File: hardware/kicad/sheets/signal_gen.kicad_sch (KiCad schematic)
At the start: 32 parts, among them U3 SG-8002CA-PH 25MHz, U4 AD9833BRMZ, U5 OPA1656ID, U6 AD633JRZ-R7, U7 MCP4921-E/SN, U8 LM4040DBZ-2.5, U9 OPA188ID

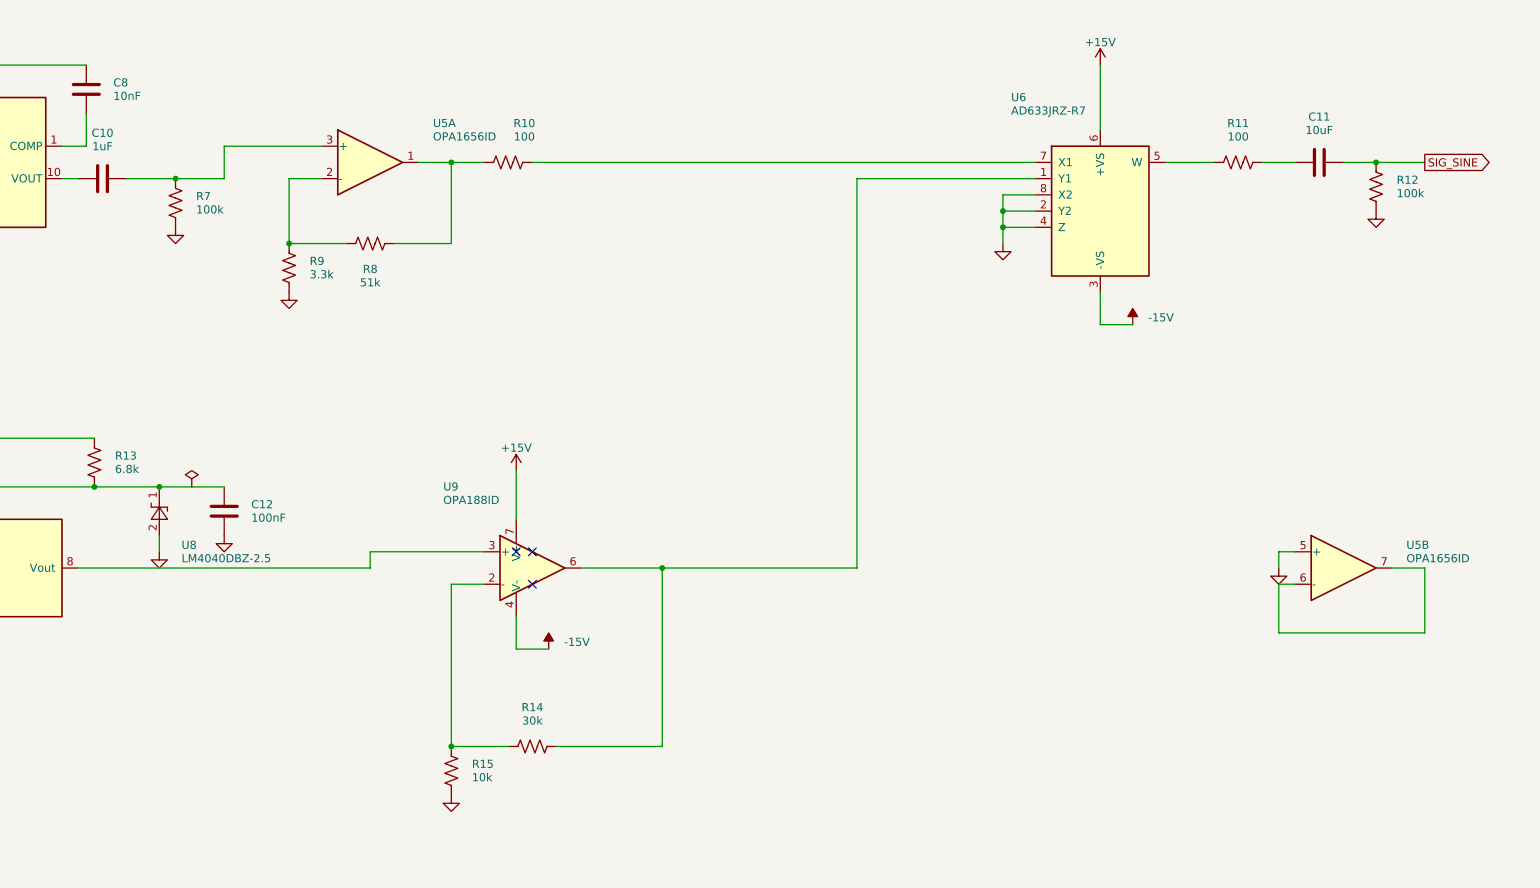
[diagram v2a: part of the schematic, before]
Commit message: KiCad schematic: INA239, ADS1220, SC18IS604 bridge, relay driver, test points
- system_current: INA237 -> INA239 (SPI, CS GPIO3) with the 49.9 ohm / 470 nF
  input filter, power LED and ALERT LED; VBUS shares the filtered IN- node.
- cold_head: ADS122C04 -> ADS1220 (SPI, CS GPIO44).
- i2c_bridge (new): SC18IS604 SPI-to-I2C bridge for the EMC2303, with a
  74LVC1G125 gating its MISO onto the shared bus.
- compressor_relay (new): GPIO16 high-side switch sharing one generator
  function with the amplifier REM switch.
- debug (new): about 40 test points and rail LEDs (the isolated rail LED
  returns to ISO_GND).
- ISO7741 -> ACS37800 SPI lines are straight wires (pins reordered on the
  symbol); USB_VBUS is one wire plus a naming label.
- Custom symbols for INA239, ADS1220, SC18IS604; datasheet rules 117 -> 162;
  GPIO map checks updated. ERC 0.

Co-Authored-By: Claude Sonnet 5.5 <noreply@anthropic.com>
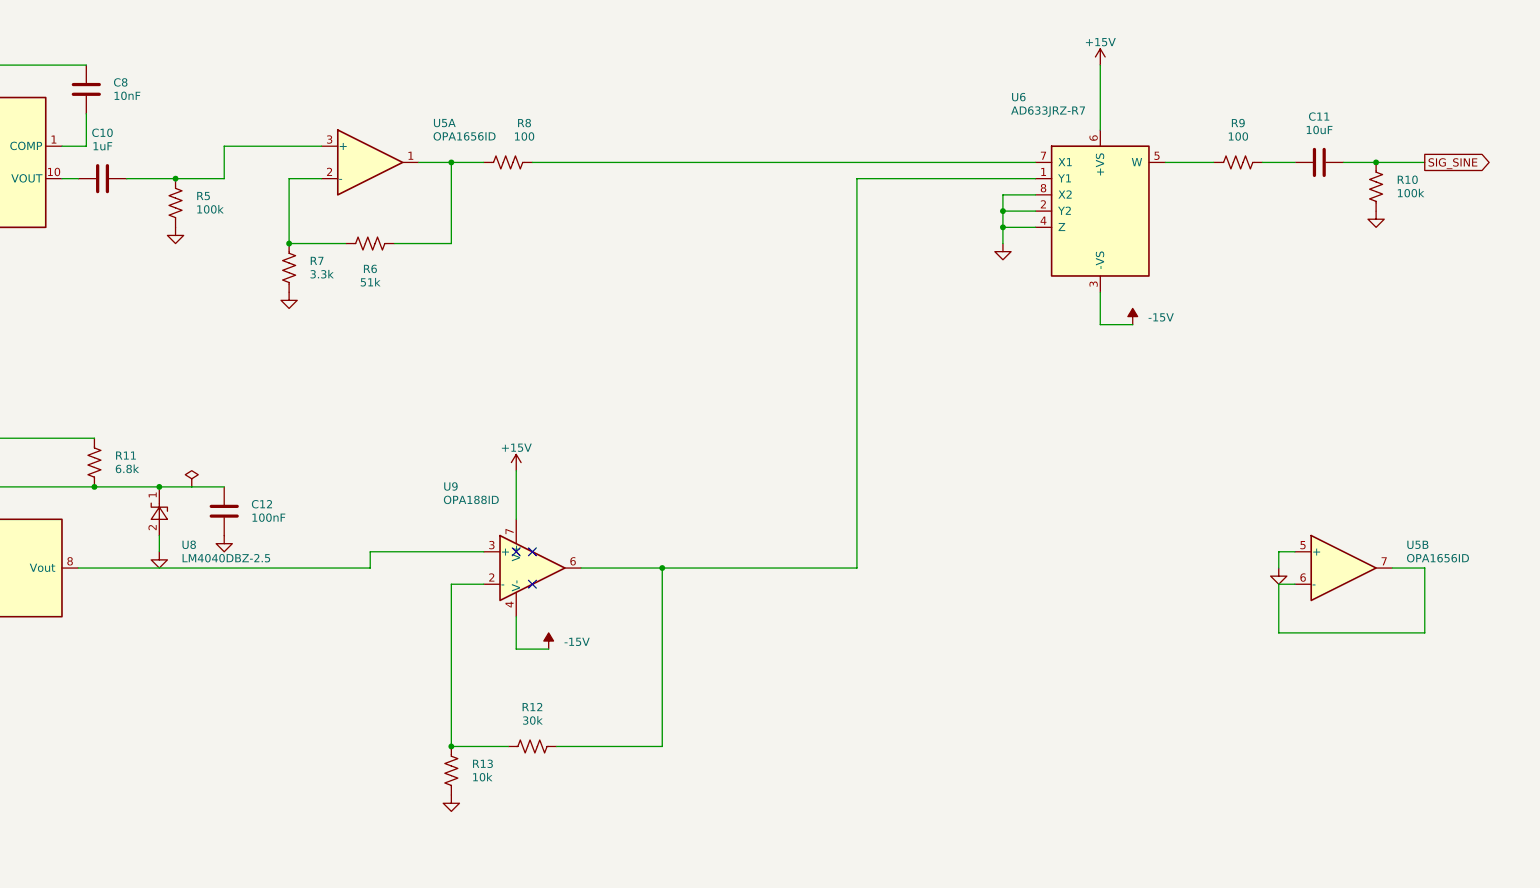
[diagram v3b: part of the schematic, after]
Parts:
- removed C15, C21: 10uF, Capacitor_SMD:C_0805_2012Metric, symbol Device:C
- removed C16, C22: 100nF, Capacitor_SMD:C_0603_1608Metric, symbol Device:C
- removed R14: 30k, Resistor_SMD:R_0603_1608Metric, symbol Device:R_US
- removed R15: 10k, Resistor_SMD:R_0603_1608Metric, symbol Device:R_US
- removed R9: 3.3k, Resistor_SMD:R_0603_1608Metric, symbol Device:R_US
- removed unit 2 of U5
- removed U7: MCP4921-E/SN, Package_SO:SOIC-8_3.9x4.9mm_P1.27mm, symbol cryocooler:MCP4921
- removed U9: OPA188ID, Package_SO:SOIC-8_3.9x4.9mm_P1.27mm, symbol Amplifier_Operational:OPA188xxD
- added C12, C13, C14, C19, C20: 100nF, Capacitor_SMD:C_0603_1608Metric, symbol Device:C
- added C8: 10nF, Capacitor_SMD:C_0603_1608Metric, symbol Device:C
- added R12: 30k, Resistor_SMD:R_0603_1608Metric, symbol Device:R_US
- added U4: AD9833BRMZ, Package_SO:MSOP-10_3x3mm_P0.5mm, symbol Interface:AD9833xRM
- added unit 1 of U5
- added U6: AD633JRZ-R7, Package_SO:SOIC-8_3.9x4.9mm_P1.27mm, symbol cryocooler:AD633JRZ-R7
- C10: renamed from C8; value 10nF -> 1uF; footprint Capacitor_SMD:C_0603_1608Metric -> Capacitor_SMD:C_0805_2012Metric
- C15: renamed from C13; value 100nF -> 10uF; footprint Capacitor_SMD:C_0603_1608Metric -> Capacitor_SMD:C_0805_2012Metric
- C21: renamed from C19; value 100nF -> 10uF; footprint Capacitor_SMD:C_0603_1608Metric -> Capacitor_SMD:C_0805_2012Metric
- C9: renamed from U4; value AD9833BRMZ -> 100nF; footprint Package_SO:MSOP-10_3x3mm_P0.5mm -> Capacitor_SMD:C_0603_1608Metric; symbol Interface:AD9833xRM -> Device:C
- R10: value 100 -> 100k
- R11: renamed from R12; value 100k -> 6.8k
- R13: value 6.8k -> 10k
- R5: renamed from C9; value 100nF -> 100k; footprint Capacitor_SMD:C_0603_1608Metric -> Resistor_SMD:R_0603_1608Metric; symbol Device:C -> Device:R_US
- R6: renamed from C10; value 1uF -> 51k; footprint Capacitor_SMD:C_0805_2012Metric -> Resistor_SMD:R_0603_1608Metric; symbol Device:C -> Device:R_US
- R7: value 100k -> 3.3k
- R8: renamed from U5; value OPA1656ID -> 100; footprint Package_SO:SOIC-8_3.9x4.9mm_P1.27mm -> Resistor_SMD:R_0603_1608Metric; symbol Amplifier_Operational:OPA1656ID -> Device:R_US
- R9: renamed from U6; value AD633JRZ-R7 -> 100; footprint Package_SO:SOIC-8_3.9x4.9mm_P1.27mm -> Resistor_SMD:R_0603_1608Metric; symbol cryocooler:AD633JRZ-R7 -> Device:R_US
- U5: renamed from R8; value 51k -> OPA1656ID; footprint Resistor_SMD:R_0603_1608Metric -> Package_SO:SOIC-8_3.9x4.9mm_P1.27mm; symbol Device:R_US -> Amplifier_Operational:OPA1656ID
- U7: renamed from R11; value 100 -> MCP4921-E/SN; footprint Resistor_SMD:R_0603_1608Metric -> Package_SO:SOIC-8_3.9x4.9mm_P1.27mm; symbol Device:R_US -> cryocooler:MCP4921
- U9: renamed from C12; value 100nF -> OPA188ID; footprint Capacitor_SMD:C_0603_1608Metric -> Package_SO:SOIC-8_3.9x4.9mm_P1.27mm; symbol Device:C -> Amplifier_Operational:OPA188xxD
- renumbered C14 to C16, C20 to C22
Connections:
- net +15V: now also C16.1, C22.1, U9.7 (V+), U6.6 (+VS); no longer R9.6 (+VS)
- net +3V3: now also C21.1, R11.1, U7.1 (Vdd), C20.1; no longer C22.1, R13.1
- net +5V: now also C13.1, C14.1, C8.1, U4.2 (VDD); no longer C10.1, C16.1, C9.2 (VDD)
- net -15V: now also U9.4 (V-), C19.1, U6.3 (-VS); no longer C21.1, R9.3 (-VS)
- net AD9833_FSYNC: now also U4.8 (~{FSYNC}); no longer C9.8 (~{FSYNC})
- net GND: now also C9.2, R10.2, R13.2, U5.5 (+), U7.5 (~{LDAC}), U7.7 (Vss), C12.2, C13.2, C14.2, C19.2, C20.2, U4.4 (DGND), U4.9 (AGND), U6.2 (Y2), U6.4 (Z), U6.8 (X2); no longer C9.4 (DGND), C9.9 (AGND), R11.2, R9.2 (Y2), R9.4 (Z), R9.8 (X2), U9.2
- net MCP4921_CS: now also U7.2 (~{CS})
- net SIG_SINE: now also R10.1; no longer R11.1
- net SPI_MOSI: now also U7.4 (SDI), U4.6 (SDATA); no longer C9.6 (SDATA)
- net SPI_SCK: now also U7.3 (SCK), U4.7 (SCLK); no longer C9.7 (SCLK)
- net at R9.1: now also U6.5 (W)
- net at R6.1: now also R7.1, U5.2 (-); no longer C9.10 (VOUT)
- net at R8.2: now also U6.7 (X1); no longer U5.1
- net at C9.1: now also U4.3 (CAP/2.5V); no longer C10.2
- net at R5.1: now also C10.2, U5.3 (+); no longer C9.3 (CAP/2.5V)
- net at U3.3 (OUT): now also U4.5 (MCLK); no longer C9.5 (MCLK)
- net at C11.1: now also R9.2; no longer U7.2
- new net: C8.2, U4.1 (COMP)
- new net: C10.1, U4.10 (VOUT)
- new net: R6.2, R8.1, U5.1
- new net: R12.1, R13.1, U9.2 (-)
- new net: R12.2, U6.1 (Y1), U9.6
- new net: C12.1, R11.2, U7.6 (Vref), U8.1 (K)
- new net: U7.8 (Vout), U9.3 (+)
- new net: U5.6 (-), U5.7
- now unconnected: U9.1
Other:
- moved on the sheet: C10, C15, C16, C21, C22, R11, R7

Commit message: Add per-section supply jumpers, 8-pin IMU header and connector pin labels
- Four 1.27 mm 2-pin jumpers (JP1-JP4), each with a rail-on LED, cut the
  supply of one section for debugging: signal generator +3V3, +-15V
  generator +5V in, isolated amp-current supply +5V in, and a shared
  +3V3 net for the cooling chips (EMC2303, RTD ADC, I2C bridge).
- J14 is now an 8-pin JST XH in the Adafruit LSM6DSOX pad order
  (VIN, GND, SCL, SDA, DO, CS, I1, I2); firmware pin comments updated.
- Pin-function labels beside every connector, "RAILS ±15V" box title.
- Board re-placed and re-routed (130 x 110 mm); DRC 0 errors, 0 unconnected,
  ERC 0, 173 datasheet rules pass. BOM, READMEs, Gerbers and renders
  regenerated; link_usb_vbus.py now adapts to the routed layout.

Co-Authored-By: Claude Sonnet 5.5 <noreply@anthropic.com>
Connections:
- net +3V3 renamed +3V3_SG
